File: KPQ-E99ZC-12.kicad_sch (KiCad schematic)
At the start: 23 parts, among them J1 USB, J2 Chassis, J3 SWD, J4 Edge Connector, J5 Alternate Connector, SW1 BOOT, U1 USBLC6-2SC6, U2 XC6206P332MR-G, U3 STM32C071KBT6

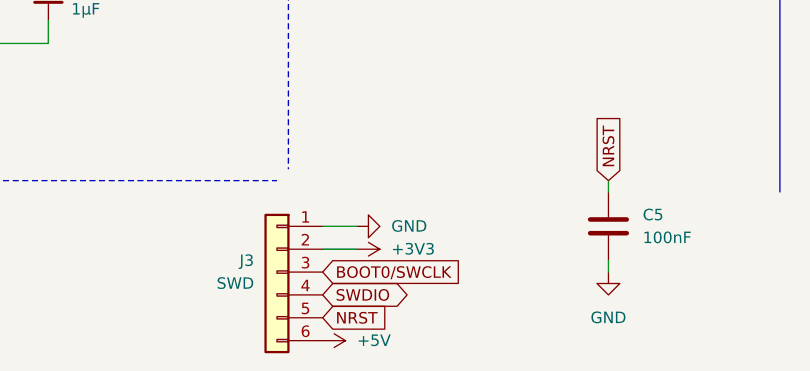
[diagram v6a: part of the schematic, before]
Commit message: Various tweaks, mostly to silkscreen
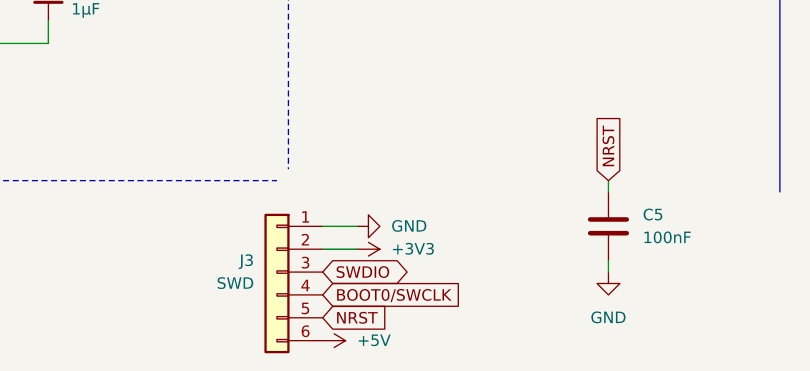
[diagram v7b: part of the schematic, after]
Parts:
- J3: footprint Project_Library:PinHeader_1x06_P2.54mm_Vertical -> Connector_PinHeader_2.54mm:PinHeader_1x06_P2.54mm_Vertical; P3 CLK -> I/O; P4 I/O -> CLK
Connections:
- net BOOT0/SWCLK: now also J3.4 (Pin_4); no longer J3.3 (Pin_3)
- net SWDIO: now also J3.3 (Pin_3); no longer J3.4 (Pin_4)
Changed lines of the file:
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@@
 	(global_label "BOOT0{slash}SWCLK"
 		(shape input)
-		(at 83.82 185.42 0)
+		(at 83.82 187.96 0)
 		(fields_autoplaced yes)
 		(effects
@@
 		)
 		(property "Intersheetrefs" "${INTERSHEET_REFS}"
-			(at 98.3153 185.42 0)
+			(at 98.3153 187.96 0)
 			(effects
 				(font
@@
 	(global_label "SWDIO"
 		(shape bidirectional)
-		(at 83.82 187.96 0)
+		(at 83.82 185.42 0)
 		(fields_autoplaced yes)
 		(effects
@@
 		)
 		(property "Intersheetrefs" "${INTERSHEET_REFS}"
-			(at 93.0429 187.96 0)
+			(at 93.0429 185.42 0)
 			(effects
 				(font
@@
 			)
 		)
-		(property "Footprint" "Project_Library:PinHeader_1x06_P2.54mm_Vertical"
+		(property "Footprint" "Connector_PinHeader_2.54mm:PinHeader_1x06_P2.54mm_Vertical"
 			(at 78.74 185.42 0)
 			(effects
@@
 			)
 		)
-		(property "P3" "CLK"
+		(property "P3" "I/O"
 			(at 78.74 185.42 0)
 			(effects
@@
 			)
 		)
-		(property "P4" "I/O"
+		(property "P4" "CLK"
 			(at 78.74 185.42 0)
 			(effects

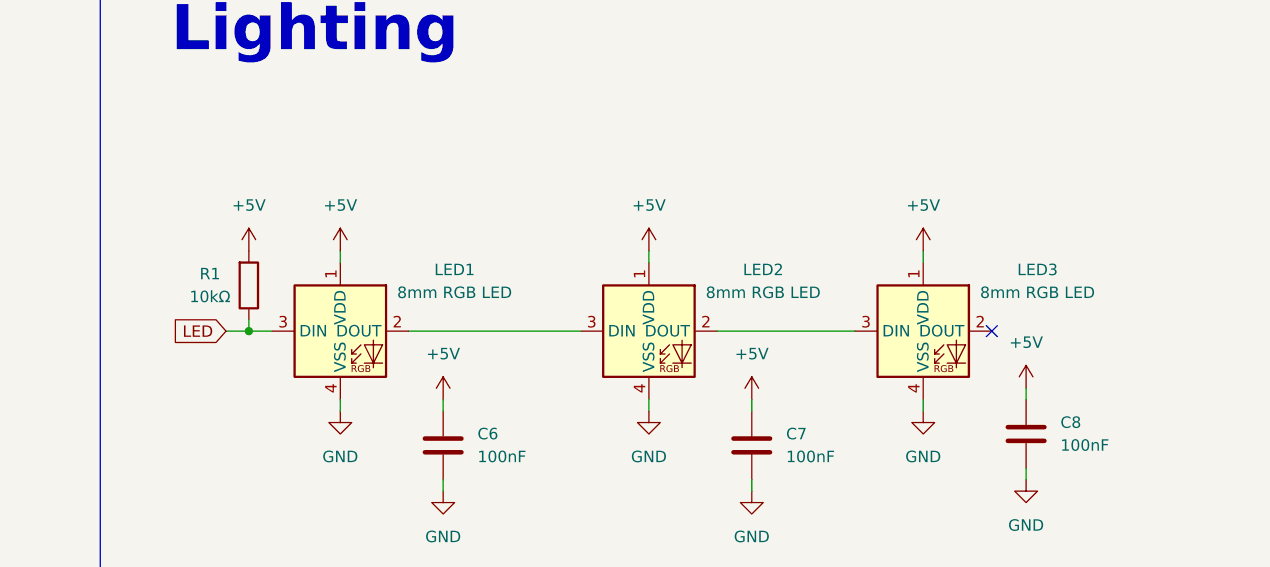
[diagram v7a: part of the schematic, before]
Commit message: Use correct symbol for RBG LEDs
!!
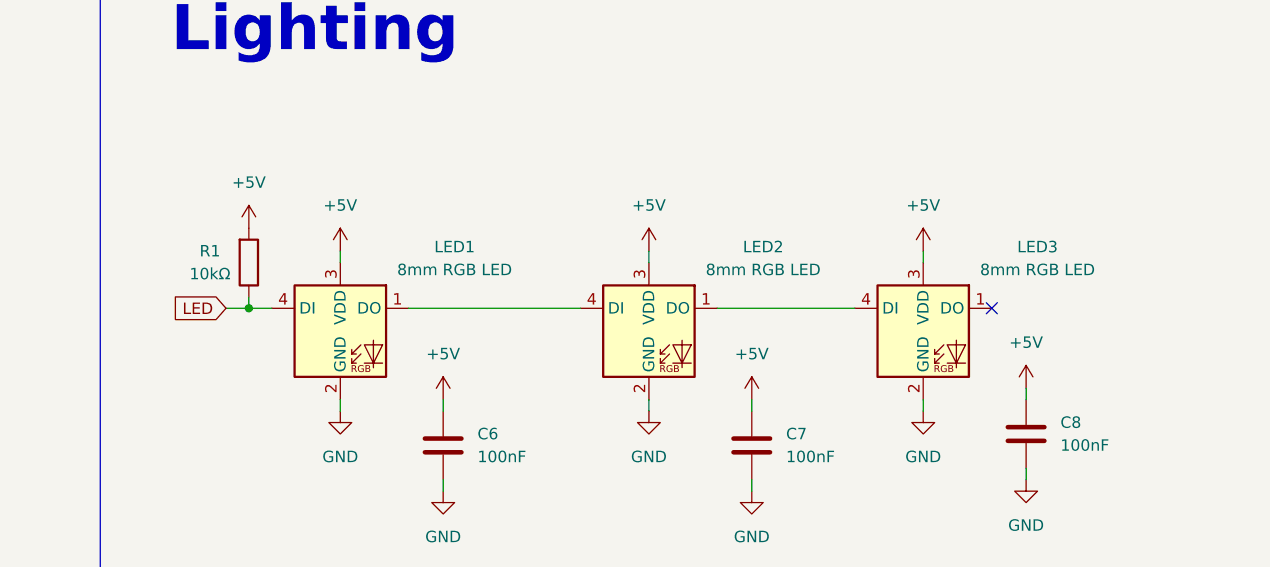
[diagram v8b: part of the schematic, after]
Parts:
- LED1, LED2, LED3: symbol PCM_marbastlib-various:SK6812MINI-E -> LED:APA-106-F5
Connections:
- net +5V: now also LED1.3 (VDD), LED2.3 (VDD), LED3.3 (VDD); no longer LED1.1 (VDD), LED2.1 (VDD), LED3.1 (VDD)
- net GND: now also LED1.2 (GND), LED2.2 (GND), LED3.2 (GND); no longer LED1.4 (VSS), LED2.4 (VSS), LED3.4 (VSS)
- net LED: now also LED1.4 (DI); no longer LED1.3 (DIN)
- new net: LED2.1 (DO), LED3.4 (DI)
- new net: LED1.1 (DO), LED2.4 (DI)
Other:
- moved on the sheet: R1
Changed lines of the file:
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@@
 	)
 	(junction
-		(at 242.57 96.52)
+		(at 242.57 93.98)
 		(diameter 0)
 		(color 0 0 0 0)
 	)
 	(no_connect
-		(at 325.12 96.52)
+		(at 325.12 93.98)
 	)
 	(wire
@@
 	(wire
 		(pts
-			(xy 294.64 96.52) (xy 309.88 96.52)
+			(xy 294.64 93.98) (xy 309.88 93.98)
 		)
 		(stroke
@@
 	(wire
 		(pts
-			(xy 260.35 96.52) (xy 279.4 96.52)
+			(xy 260.35 93.98) (xy 279.4 93.98)
 		)
 		(stroke
@@
 	(wire
 		(pts
-			(xy 240.03 96.52) (xy 242.57 96.52)
+			(xy 240.03 93.98) (xy 242.57 93.98)
 		)
 		(stroke
@@
 	(wire
 		(pts
-			(xy 242.57 95.25) (xy 242.57 96.52)
+			(xy 242.57 92.71) (xy 242.57 93.98)
 		)
 		(stroke
@@
 	(wire
 		(pts
-			(xy 242.57 96.52) (xy 245.11 96.52)
+			(xy 242.57 93.98) (xy 245.11 93.98)
 		)
 		(stroke
@@
 	(global_label "LED"
 		(shape input)
-		(at 240.03 96.52 180)
+		(at 240.03 93.98 180)
 		(fields_autoplaced yes)
 		(effects
@@
 		)
 		(property "Intersheetrefs" "${INTERSHEET_REFS}"
-			(at 233.5977 96.52 0)
+			(at 233.5977 93.98 0)
 			(effects
 				(font
@@
 	)
 	(symbol
-		(lib_id "PCM_marbastlib-various:SK6812MINI-E")
+		(lib_id "LED:APA-106-F5")
 		(at 287.02 96.52 0)
 		(unit 1)
@@
 		(fields_autoplaced yes)
 		(property "Reference" "LED2"
-			(at 299.72 89.7123 0)
+			(at 299.72 87.1723 0)
 			(effects
 				(font
@@
 		)
 		(property "Value" "8mm RGB LED"
-			(at 299.72 92.2523 0)
+			(at 299.72 89.7123 0)
 			(effects
 				(font
@@
 		)
 		(property "Footprint" "LED_THT:LED_D5.0mm-4_RGB"
-			(at 287.02 96.52 0)
+			(at 288.29 104.14 0)
 			(effects
 				(font
 					(size 1.27 1.27)
 				)
+				(justify left top)
 				(hide yes)
 			)
 		)
-		(property "Datasheet" ""
-			(at 287.02 96.52 0)
+		(property "Datasheet" "https://cdn.sparkfun.com/datasheets/Components/LED/COM-12877.pdf"
+			(at 289.56 106.045 0)
 			(effects
 				(font
 					(size 1.27 1.27)
 				)
+				(justify left top)
 				(hide yes)
 			)
 		)
-		(property "Description" "Reverse mount adressable LED (WS2812 protocol)"
+		(property "Description" "RGB LED with integrated controller, 5mm Package"
 			(at 287.02 96.52 0)
 			(effects
@@
 	(symbol
 		(lib_id "power:+5V")
-		(at 242.57 87.63 0)
+		(at 242.57 85.09 0)
 		(unit 1)
 		(exclude_from_sim no)
@@
 		(fields_autoplaced yes)
 		(property "Reference" "#PWR019"
-			(at 242.57 91.44 0)
+			(at 242.57 88.9 0)
 			(effects
 				(font
@@
 		)
 		(property "Value" "+5V"
-			(at 242.57 82.55 0)
+			(at 242.57 80.01 0)
 			(effects
 				(font
@@
 		)
 		(property "Footprint" ""
-			(at 242.57 87.63 0)
+			(at 242.57 85.09 0)
 			(effects
 				(font
@@
 		)
 		(property "Datasheet" ""
-			(at 242.57 87.63 0)
+			(at 242.57 85.09 0)
 			(effects
 				(font
@@
 		)
 		(property "Description" "Power symbol creates a global label with name \"+5V\""
-			(at 242.57 87.63 0)
+			(at 242.57 85.09 0)
 			(effects
 				(font
@@
 	(symbol
 		(lib_id "Device:R")
-		(at 242.57 91.44 0)
+		(at 242.57 88.9 0)
 		(mirror x)
 		(unit 1)
@@
 		(dnp no)
 		(property "Reference" "R1"
-			(at 238.252 90.17 0)
+			(at 238.252 87.63 0)
 			(effects
 				(font
@@
 		)
 		(property "Value" "10kΩ"
-			(at 238.252 92.71 0)
+			(at 238.252 90.17 0)
 			(effects
 				(font
@@
 		)
 		(property "Footprint" "Resistor_THT:R_Axial_DIN0207_L6.3mm_D2.5mm_P7.62mm_Horizontal"
-			(at 240.792 91.44 90)
+			(at 240.792 88.9 90)
 			(effects
 				(font
@@
 		)
 		(property "Datasheet" "~"
-			(at 242.57 91.44 0)
+			(at 242.57 88.9 0)
 			(effects
 				(font
@@
 		)
 		(property "Description" "Resistor"
-			(at 242.57 91.44 0)
+			(at 242.57 88.9 0)
 			(effects
 				(font
@@
 	)
 	(symbol
-		(lib_id "PCM_marbastlib-various:SK6812MINI-E")
+		(lib_id "LED:APA-106-F5")
 		(at 317.5 96.52 0)
 		(unit 1)
@@
 		(fields_autoplaced yes)
 		(property "Reference" "LED3"
-			(at 330.2 89.7123 0)
+			(at 330.2 87.1723 0)
 			(effects
 				(font
@@
 		)
 		(property "Value" "8mm RGB LED"
-			(at 330.2 92.2523 0)
+			(at 330.2 89.7123 0)
 			(effects
 				(font
@@
 		)
 		(property "Footprint" "LED_THT:LED_D5.0mm-4_RGB"
-			(at 317.5 96.52 0)
+			(at 318.77 104.14 0)
 			(effects
 				(font
 					(size 1.27 1.27)
 				)
+				(justify left top)
 				(hide yes)
 			)
 		)
-		(property "Datasheet" ""
-			(at 317.5 96.52 0)
+		(property "Datasheet" "https://cdn.sparkfun.com/datasheets/Components/LED/COM-12877.pdf"
+			(at 320.04 106.045 0)
 			(effects
 				(font
 					(size 1.27 1.27)
 				)
+				(justify left top)
 				(hide yes)
 			)
 		)
-		(property "Description" "Reverse mount adressable LED (WS2812 protocol)"
+		(property "Description" "RGB LED with integrated controller, 5mm Package"
 			(at 317.5 96.52 0)
 			(effects
@@
 	)
 	(symbol
-		(lib_id "PCM_marbastlib-various:SK6812MINI-E")
+		(lib_id "LED:APA-106-F5")
 		(at 252.73 96.52 0)
 		(unit 1)
@@
 		(fields_autoplaced yes)
 		(property "Reference" "LED1"
-			(at 265.43 89.7123 0)
+			(at 265.43 87.1723 0)
 			(effects
 				(font
@@
 		)
 		(property "Value" "8mm RGB LED"
-			(at 265.43 92.2523 0)
+			(at 265.43 89.7123 0)
 			(effects
 				(font
@@
 		)
 		(property "Footprint" "LED_THT:LED_D5.0mm-4_RGB"
-			(at 252.73 96.52 0)
+			(at 254 104.14 0)
 			(effects
 				(font
 					(size 1.27 1.27)
 				)
+				(justify left top)
 				(hide yes)
 			)
 		)
-		(property "Datasheet" ""
-			(at 252.73 96.52 0)
+		(property "Datasheet" "https://cdn.sparkfun.com/datasheets/Components/LED/COM-12877.pdf"
+			(at 255.27 106.045 0)
 			(effects
 				(font
 					(size 1.27 1.27)
 				)
+				(justify left top)
 				(hide yes)
 			)
 		)
-		(property "Description" "Reverse mount adressable LED (WS2812 protocol)"
+		(property "Description" "RGB LED with integrated controller, 5mm Package"
 			(at 252.73 96.52 0)
 			(effects
